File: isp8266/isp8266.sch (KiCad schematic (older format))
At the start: 65 parts, among them J1 Bottom, J10 BAT2, J11 USB_C_Receptacle_USB2.0, J12 F1, J2 Up, J7 F0, J8 BAT1, Q1 S8050, Q2 S8050, Q3 BSS138, Q4 IRLML6402, Q5 BSS138, Q6 IRLML6402, U1 CH340C, U2 AP1117-33, U3 IP5306, U4 ESP-07

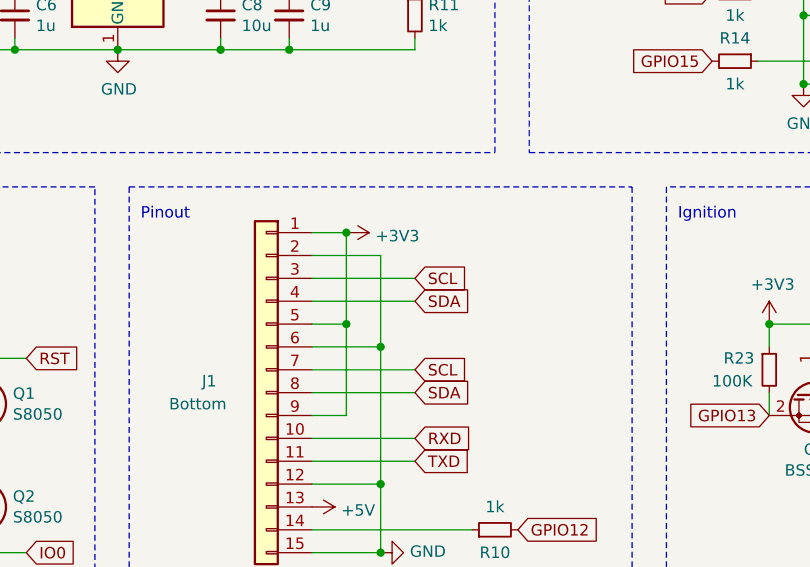
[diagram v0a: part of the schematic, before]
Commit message: Mirror IMU pin and update footprint
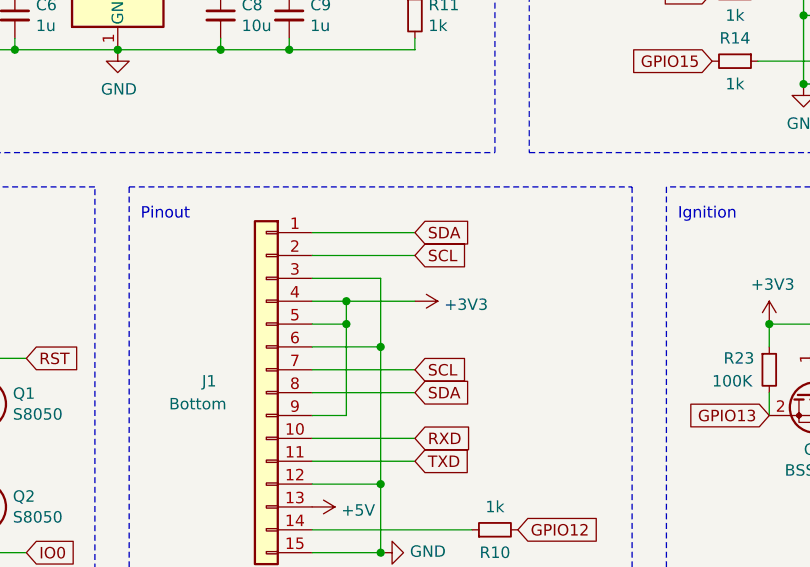
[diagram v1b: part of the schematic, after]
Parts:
- JP1: footprint Connector_PinSocket_2.54mm:PinSocket_1x03_P2.54mm_Vertical -> Connector_PinHeader_2.54mm:PinHeader_1x03_P2.54mm_Vertical
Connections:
- net +3V3: now also J1.4 (Pin_4); no longer J1.1 (Pin_1)
- net -BATT: now also J1.3 (Pin_3); no longer J1.2 (Pin_2)
- net SCL: now also J1.2 (Pin_2); no longer J1.3 (Pin_3)
- net SDA: now also J1.1 (Pin_1); no longer J1.4 (Pin_4)
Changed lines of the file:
@@
 F 0 "JP1" V 9954 5336 50  0000 L CNN
 F 1 "IGN_VOL" V 10045 5336 50  0000 L CNN
-F 2 "Connector_PinSocket_2.54mm:PinSocket_1x03_P2.54mm_Vertical" H 10000 5250 50  0001 C CNN
+F 2 "Connector_PinHeader_2.54mm:PinHeader_1x03_P2.54mm_Vertical" H 10000 5250 50  0001 C CNN
 F 3 "~" H 10000 5250 50  0001 C CNN
 	1    10000 5250
@@
 	7150 3400 7300 3400
 Connection ~ 7150 3100
-Connection ~ 5000 4250
-Wire Wire Line
-	4850 4250 5000 4250
+Wire Wire Line
+	4850 4550 5000 4550
 Text GLabel 5300 5150 2    50   Input ~ 0
 RXD
@@
 Text GLabel 5750 5550 2    50   Input ~ 0
 GPIO12
-Text GLabel 5300 4450 2    50   Input ~ 0
+Text GLabel 5300 4350 2    50   Input ~ 0
 SCL
-Text GLabel 5300 4550 2    50   Input ~ 0
+Text GLabel 5300 4250 2    50   Input ~ 0
 SDA
 $Comp
@@
 SDA
 Wire Wire Line
-	4850 4450 5300 4450
-Wire Wire Line
-	5300 4550 4850 4550
+	4850 4350 5300 4350
+Wire Wire Line
+	5300 4250 4850 4250
 Wire Wire Line
 	4850 4850 5300 4850
@@
 	4850 4950 5300 4950
 Wire Wire Line
-	4850 4350 5150 4350
-Wire Wire Line
-	5150 4350 5150 4750
-Wire Wire Line
 	4850 4650 5000 4650
 Wire Wire Line
-	5000 4650 5000 4250
-Wire Wire Line
 	4850 4750 5150 4750
-Connection ~ 5150 4750
 Wire Wire Line
 	5150 4750 5150 5350
@@
 Wire Wire Line
 	5000 5050 5000 4650
-Connection ~ 5000 4650
 $Comp
 L power:GND #PWR033
@@
 L power:+3V3 #PWR017
 U 1 1 63974487
-P 5000 4250
-F 0 "#PWR017" H 5000 4100 50  0001 C CNN
-F 1 "+3V3" V 5015 4378 50  0000 L CNN
-F 2 "" H 5000 4250 50  0001 C CNN
-F 3 "" H 5000 4250 50  0001 C CNN
-	1    5000 4250
+P 5300 4550
+F 0 "#PWR017" H 5300 4400 50  0001 C CNN
+F 1 "+3V3" V 5315 4678 50  0000 L CNN
+F 2 "" H 5300 4550 50  0001 C CNN
+F 3 "" H 5300 4550 50  0001 C CNN
+	1    5300 4550
 	0    1    1    0
 $EndComp
@@
 	1    0    0    -1
 $EndComp
+Wire Wire Line
+	5000 4650 5000 4550
+Connection ~ 5000 4650
+Wire Wire Line
+	4850 4450 5150 4450
+Wire Wire Line
+	5150 4450 5150 4750
+Connection ~ 5150 4750
+Wire Wire Line
+	5300 4550 5000 4550
+Connection ~ 5000 4550
 $EndSCHEMATC

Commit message: Change switch position and battery connector
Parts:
- J10, J8: footprint Connector_Molex:Molex_KK-254_AE-6410-02A_1x02_P2.54mm_Vertical -> Connector_JST:JST_XH_B2B-XH-A_1x02_P2.50mm_Vertical
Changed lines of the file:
@@
 F 0 "J8" H 7280 1692 50  0000 L CNN
 F 1 "BAT1" H 7280 1601 50  0000 L CNN
-F 2 "Connector_Molex:Molex_KK-254_AE-6410-02A_1x02_P2.54mm_Vertical" H 7200 1700 50  0001 C CNN
+F 2 "Connector_JST:JST_XH_B2B-XH-A_1x02_P2.50mm_Vertical" H 7200 1700 50  0001 C CNN
 F 3 "~" H 7200 1700 50  0001 C CNN
 	1    7200 1700
@@
 F 0 "J10" H 10280 4392 50  0000 L CNN
 F 1 "BAT2" H 10280 4301 50  0000 L CNN
-F 2 "Connector_Molex:Molex_KK-254_AE-6410-02A_1x02_P2.54mm_Vertical" H 10200 4400 50  0001 C CNN
+F 2 "Connector_JST:JST_XH_B2B-XH-A_1x02_P2.50mm_Vertical" H 10200 4400 50  0001 C CNN
 F 3 "~" H 10200 4400 50  0001 C CNN
 	1    10200 4400
